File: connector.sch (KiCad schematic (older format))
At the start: 9 parts, among them J4 Conn_01x08, J5 Conn_01x06, J6 Conn_01x10, J7 Conn_01x08, U5 TA48L033

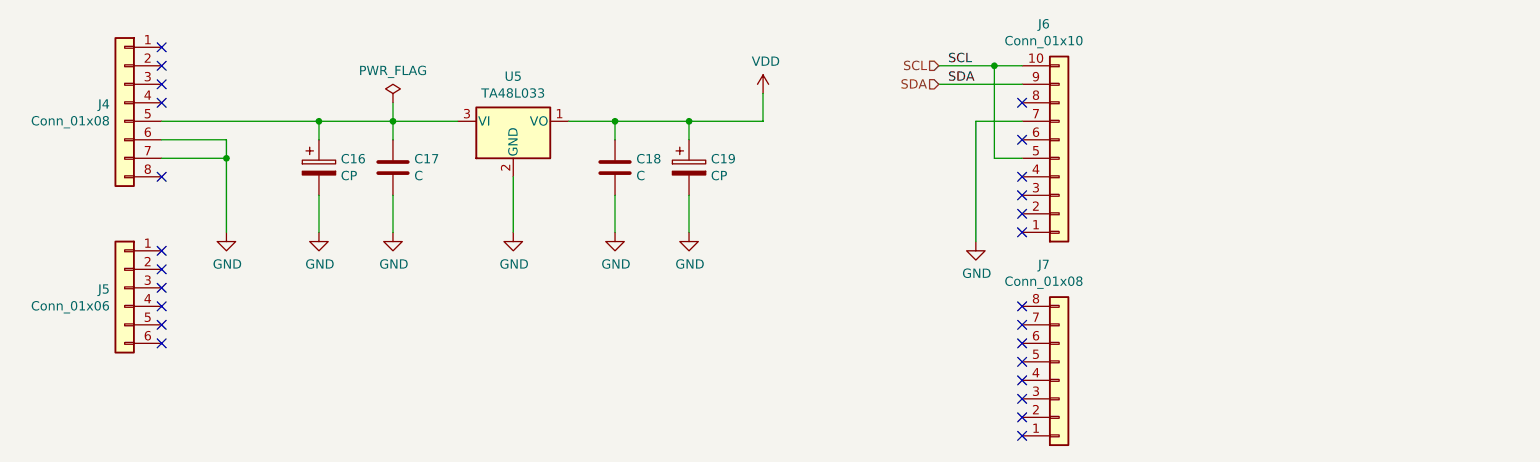
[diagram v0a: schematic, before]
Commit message: Schematics are almost done.
Audio jack is not yet.
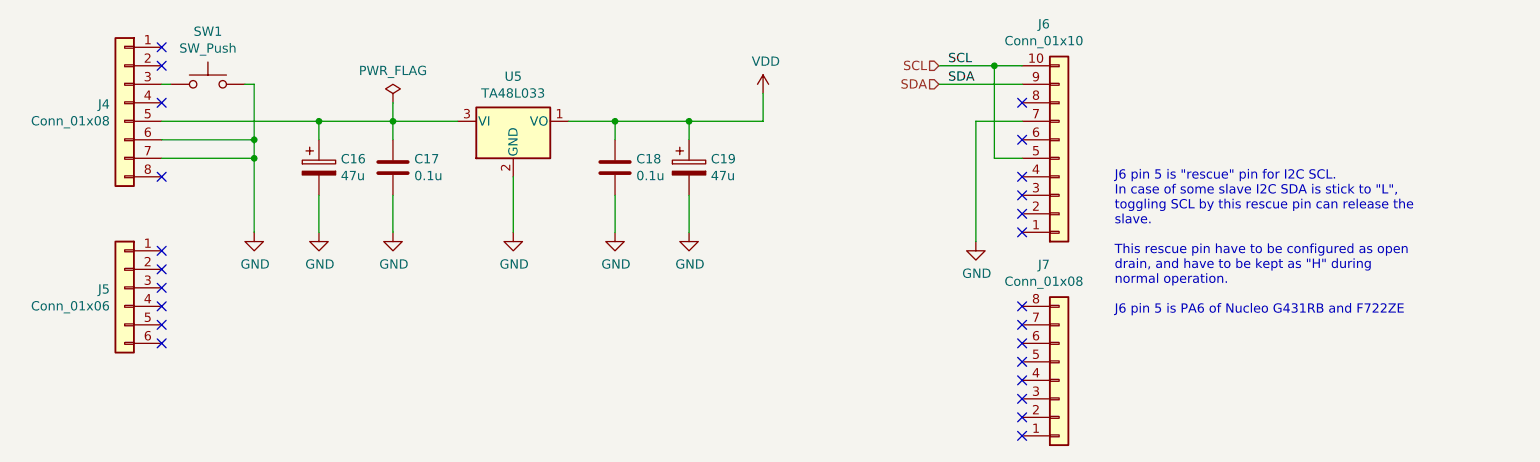
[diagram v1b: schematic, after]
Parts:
- added SW1: SW_Push, Buttons_Switches_THT:SW_PUSH_6mm_h5mm, symbol Switch:SW_Push
- C16, C19: value CP -> 47u; footprint (none) -> Capacitors_THT:CP_Radial_D8.0mm_P2.50mm
- C17, C18: value C -> 0.1u; footprint (none) -> Capacitors_THT:C_Disc_D4.7mm_W2.5mm_P5.00mm
- J4, J7: footprint (none) -> Pin_Headers:Pin_Header_Straight_1x08_Pitch2.54mm
- J5: footprint (none) -> Pin_Headers:Pin_Header_Straight_1x06_Pitch2.54mm
- J6: footprint (none) -> Pin_Headers:Pin_Header_Straight_1x10_Pitch2.54mm
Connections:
- net GND: now also SW1.2
- net at J4.3 (Pin_3): now also SW1.1
- no-connect marks 25 -> 24
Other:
- note added: "J6 pin 5 is "rescue" pin for I2C SCL.\nIn case of some slave I2C SDA is stick to "L", \ntoggling SCL by this rescue pin can release the \nslave. \n\nThis rescue pin have to be configured as open \ndrain, and have to be kept as "H" during \nnormal operation. \n\nJ6 pin 5 is PA6 of Nucleo G431RB and F722ZE"
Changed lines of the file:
@@
 F 0 "J4" H 2030 1942 50  0000 L CNN
 F 1 "Conn_01x08" H 2030 1851 50  0000 L CNN
-F 2 "" H 1950 1950 50  0001 C CNN
+F 2 "Pin_Headers:Pin_Header_Straight_1x08_Pitch2.54mm" H 1950 1950 50  0001 C CNN
 F 3 "~" H 1950 1950 50  0001 C CNN
 	1    1950 1950
@@
 F 0 "J5" H 2030 2942 50  0000 L CNN
 F 1 "Conn_01x06" H 2030 2851 50  0000 L CNN
-F 2 "" H 1950 2950 50  0001 C CNN
+F 2 "Pin_Headers:Pin_Header_Straight_1x06_Pitch2.54mm" H 1950 2950 50  0001 C CNN
 F 3 "~" H 1950 2950 50  0001 C CNN
 	1    1950 2950
@@
 F 0 "J7" H 6918 2825 50  0000 C CNN
 F 1 "Conn_01x08" H 6918 2916 50  0000 C CNN
-F 2 "" H 7000 3450 50  0001 C CNN
+F 2 "Pin_Headers:Pin_Header_Straight_1x08_Pitch2.54mm" H 7000 3450 50  0001 C CNN
 F 3 "~" H 7000 3450 50  0001 C CNN
 	1    7000 3450
@@
 F 0 "J6" H 6918 1525 50  0000 C CNN
 F 1 "Conn_01x10" H 6918 1616 50  0000 C CNN
-F 2 "" H 7000 2250 50  0001 C CNN
+F 2 "Pin_Headers:Pin_Header_Straight_1x10_Pitch2.54mm" H 7000 2250 50  0001 C CNN
 F 3 "~" H 7000 2250 50  0001 C CNN
 	1    7000 2250
@@
 P 3400 2300
 F 0 "C17" H 3515 2346 50  0000 L CNN
-F 1 "C" H 3515 2255 50  0000 L CNN
-F 2 "" H 3438 2150 50  0001 C CNN
+F 1 "0.1u" H 3515 2255 50  0000 L CNN
+F 2 "Capacitors_THT:C_Disc_D4.7mm_W2.5mm_P5.00mm" H 3438 2150 50  0001 C CNN
 F 3 "~" H 3400 2300 50  0001 C CNN
 	1    3400 2300
@@
 P 3000 2300
 F 0 "C16" H 3118 2346 50  0000 L CNN
-F 1 "CP" H 3118 2255 50  0000 L CNN
-F 2 "" H 3038 2150 50  0001 C CNN
+F 1 "47u" H 3118 2255 50  0000 L CNN
+F 2 "Capacitors_THT:CP_Radial_D8.0mm_P2.50mm" H 3038 2150 50  0001 C CNN
 F 3 "~" H 3000 2300 50  0001 C CNN
 	1    3000 2300
@@
 P 4600 2300
 F 0 "C18" H 4715 2346 50  0000 L CNN
-F 1 "C" H 4715 2255 50  0000 L CNN
-F 2 "" H 4638 2150 50  0001 C CNN
+F 1 "0.1u" H 4715 2255 50  0000 L CNN
+F 2 "Capacitors_THT:C_Disc_D4.7mm_W2.5mm_P5.00mm" H 4638 2150 50  0001 C CNN
 F 3 "~" H 4600 2300 50  0001 C CNN
 	1    4600 2300
@@
 P 5000 2300
 F 0 "C19" H 5118 2346 50  0000 L CNN
-F 1 "CP" H 5118 2255 50  0000 L CNN
-F 2 "" H 5038 2150 50  0001 C CNN
+F 1 "47u" H 5118 2255 50  0000 L CNN
+F 2 "Capacitors_THT:CP_Radial_D8.0mm_P2.50mm" H 5038 2150 50  0001 C CNN
 F 3 "~" H 5000 2300 50  0001 C CNN
 	1    5000 2300
@@
 	2150 2050 3000 2050
 Wire Wire Line
-	2150 2150 2500 2150
-Wire Wire Line
-	2500 2150 2500 2250
-Wire Wire Line
-	2150 2250 2500 2250
-Connection ~ 2500 2250
-Wire Wire Line
-	2500 2250 2500 2650
+	2150 2150 2650 2150
+Wire Wire Line
+	2650 2150 2650 2250
+Wire Wire Line
+	2150 2250 2650 2250
+Connection ~ 2650 2250
+Wire Wire Line
+	2650 2250 2650 2650
 $Comp
 L power:GND #PWR0106
 U 1 1 5F10FCB9
-P 2500 2650
-F 0 "#PWR0106" H 2500 2400 50  0001 C CNN
-F 1 "GND" H 2505 2477 50  0000 C CNN
-F 2 "" H 2500 2650 50  0001 C CNN
-F 3 "" H 2500 2650 50  0001 C CNN
-	1    2500 2650
+P 2650 2650
+F 0 "#PWR0106" H 2650 2400 50  0001 C CNN
+F 1 "GND" H 2655 2477 50  0000 C CNN
+F 2 "" H 2650 2650 50  0001 C CNN
+F 3 "" H 2650 2650 50  0001 C CNN
+	1    2650 2650
 	1    0    0    -1
 $EndComp
@@
 NoConn ~ 2150 1650
 NoConn ~ 2150 1750
-NoConn ~ 2150 1850
 NoConn ~ 2150 1950
 NoConn ~ 2150 2350
@@
 Text HLabel 6350 1850 0    50   Input ~ 0
 SDA
+Wire Wire Line
+	2650 2150 2650 1850
+Wire Wire Line
+	2650 1850 2600 1850
+Connection ~ 2650 2150
+Wire Wire Line
+	2200 1850 2150 1850
+$Comp
+L Switch:SW_Push SW1
+U 1 1 5F2D861D
+P 2400 1850
+F 0 "SW1" H 2400 2135 50  0000 C CNN
+F 1 "SW_Push" H 2400 2044 50  0000 C CNN
+F 2 "Buttons_Switches_THT:SW_PUSH_6mm_h5mm" H 2400 2050 50  0001 C CNN
+F 3 "~" H 2400 2050 50  0001 C CNN
+	1    2400 1850
+	1    0    0    -1
+$EndComp
+Text Notes 7300 3100 0    50   ~ 0
+J6 pin 5 is "rescue" pin for I2C SCL.\nIn case of some slave I2C SDA is stick to "L", \ntoggling SCL by this rescue pin can release the \nslave. \n\nThis rescue pin have to be configured as open \ndrain, and have to be kept as "H" during \nnormal operation. \n\nJ6 pin 5 is PA6 of Nucleo G431RB and F722ZE
 $EndSCHEMATC

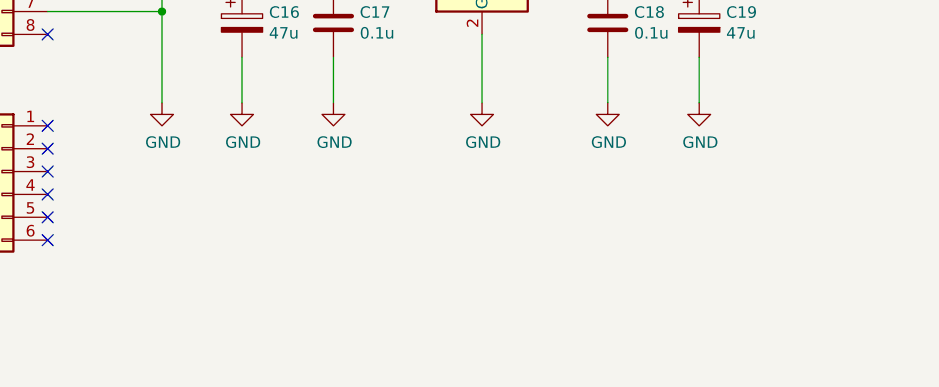
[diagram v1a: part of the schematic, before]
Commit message: Footprint done.
Added footprint of the audio jack.
The documentation link of the each IC is done.
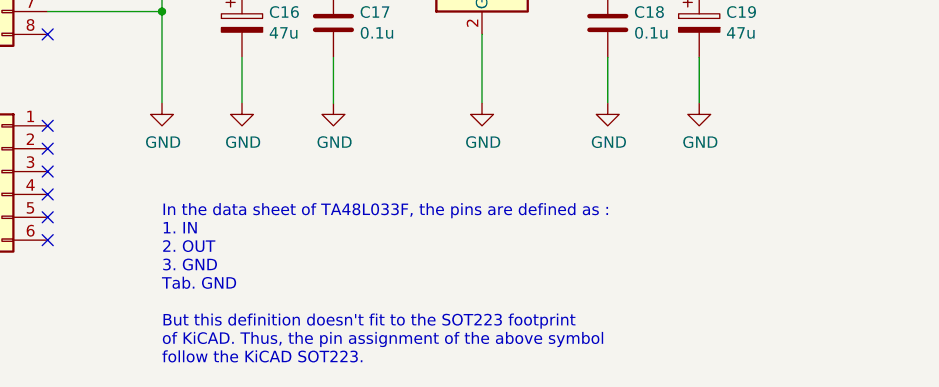
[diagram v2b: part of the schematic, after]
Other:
- note added: "In the data sheet of TA48L033F, the pins are defined as :\n1. IN\n2. OUT\n3. GND\nTab. GND\n\nBut this definition doesn't fit to the SOT223 footprint \nof KiCAD. Thus, the pin assignment of the above symbol\nfollow the KiCAD SOT223."
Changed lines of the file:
@@
 F 1 "TA48L033" H 4050 2201 50  0000 C CNN
 F 2 "TO_SOT_Packages_SMD:SOT-223-3_TabPin2" H 4050 2250 50  0001 C CNN
-F 3 "http://ww1.microchip.com/downloads/en/DeviceDoc/20005122B.pdf" H 4050 2000 50  0001 C CNN
+F 3 "https://toshiba.semicon-storage.com/jp/semiconductor/product/power-management-ics/detail.TA48L033F.html" H 4050 2000 50  0001 C CNN
 	1    4050 2050
 	1    0    0    -1
@@
 Text Notes 7300 3100 0    50   ~ 0
 J6 pin 5 is "rescue" pin for I2C SCL.\nIn case of some slave I2C SDA is stick to "L", \ntoggling SCL by this rescue pin can release the \nslave. \n\nThis rescue pin have to be configured as open \ndrain, and have to be kept as "H" during \nnormal operation. \n\nJ6 pin 5 is PA6 of Nucleo G431RB and F722ZE
+Text Notes 2650 3800 0    50   ~ 0
+In the data sheet of TA48L033F, the pins are defined as :\n1. IN\n2. OUT\n3. GND\nTab. GND\n\nBut this definition doesn't fit to the SOT223 footprint \nof KiCAD. Thus, the pin assignment of the above symbol\nfollow the KiCAD SOT223.
 $EndSCHEMATC

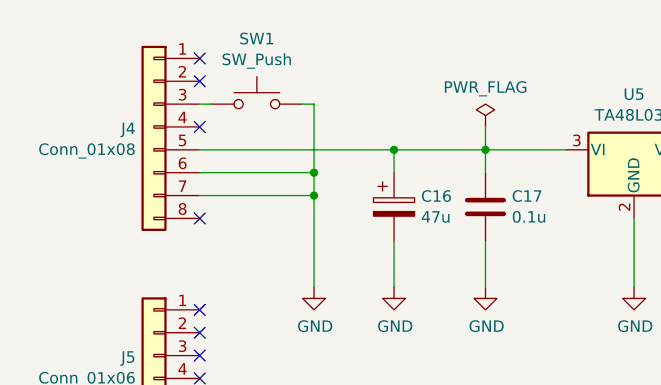
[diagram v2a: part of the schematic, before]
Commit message: All parts is on the PCB.
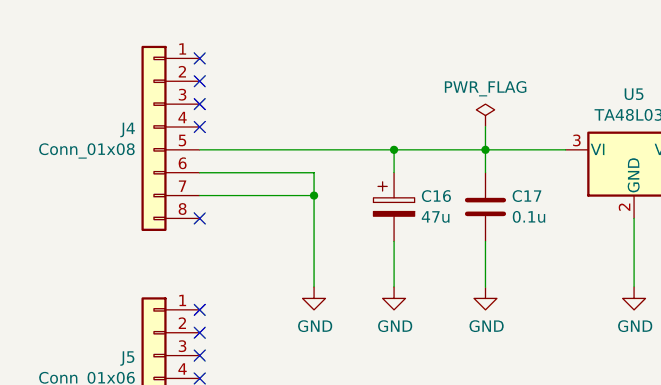
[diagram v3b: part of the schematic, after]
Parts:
- removed SW1: SW_Push, Buttons_Switches_THT:SW_PUSH_6mm_h5mm, symbol Switch:SW_Push
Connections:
- no-connect marks 24 -> 25
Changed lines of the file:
@@
 $EndComp
 $Comp
-L power:GND #PWR0101
+L power:GND #PWR032
 U 1 1 5F104015
 P 4050 2650
-F 0 "#PWR0101" H 4050 2400 50  0001 C CNN
+F 0 "#PWR032" H 4050 2400 50  0001 C CNN
 F 1 "GND" H 4055 2477 50  0000 C CNN
 F 2 "" H 4050 2650 50  0001 C CNN
@@
 $EndComp
 $Comp
-L power:GND #PWR0102
+L power:GND #PWR031
 U 1 1 5F105017
 P 3400 2650
-F 0 "#PWR0102" H 3400 2400 50  0001 C CNN
+F 0 "#PWR031" H 3400 2400 50  0001 C CNN
 F 1 "GND" H 3405 2477 50  0000 C CNN
 F 2 "" H 3400 2650 50  0001 C CNN
@@
 $EndComp
 $Comp
-L power:GND #PWR0103
+L power:GND #PWR030
 U 1 1 5F1052CF
 P 3000 2650
-F 0 "#PWR0103" H 3000 2400 50  0001 C CNN
+F 0 "#PWR030" H 3000 2400 50  0001 C CNN
 F 1 "GND" H 3005 2477 50  0000 C CNN
 F 2 "" H 3000 2650 50  0001 C CNN
@@
 $EndComp
 $Comp
-L power:GND #PWR0104
+L power:GND #PWR033
 U 1 1 5F1054A0
 P 4600 2650
-F 0 "#PWR0104" H 4600 2400 50  0001 C CNN
+F 0 "#PWR033" H 4600 2400 50  0001 C CNN
 F 1 "GND" H 4605 2477 50  0000 C CNN
 F 2 "" H 4600 2650 50  0001 C CNN
@@
 $EndComp
 $Comp
-L power:GND #PWR0105
+L power:GND #PWR034
 U 1 1 5F105733
 P 5000 2650
-F 0 "#PWR0105" H 5000 2400 50  0001 C CNN
+F 0 "#PWR034" H 5000 2400 50  0001 C CNN
 F 1 "GND" H 5005 2477 50  0000 C CNN
 F 2 "" H 5000 2650 50  0001 C CNN
@@
 	2650 2250 2650 2650
 $Comp
-L power:GND #PWR0106
+L power:GND #PWR029
 U 1 1 5F10FCB9
 P 2650 2650
-F 0 "#PWR0106" H 2650 2400 50  0001 C CNN
+F 0 "#PWR029" H 2650 2400 50  0001 C CNN
 F 1 "GND" H 2655 2477 50  0000 C CNN
 F 2 "" H 2650 2650 50  0001 C CNN
@@
 $EndComp
 $Comp
-L power:GND #PWR0107
+L power:GND #PWR036
 U 1 1 5F110343
 P 6550 2700
-F 0 "#PWR0107" H 6550 2450 50  0001 C CNN
+F 0 "#PWR036" H 6550 2450 50  0001 C CNN
 F 1 "GND" H 6555 2527 50  0000 C CNN
 F 2 "" H 6550 2700 50  0001 C CNN
@@
 NoConn ~ 6800 2150
 $Comp
-L power:VDD #PWR0108
+L power:VDD #PWR035
 U 1 1 5F116A17
 P 5400 1900
-F 0 "#PWR0108" H 5400 1750 50  0001 C CNN
+F 0 "#PWR035" H 5400 1750 50  0001 C CNN
 F 1 "VDD" H 5415 2073 50  0000 C CNN
 F 2 "" H 5400 1900 50  0001 C CNN
@@
 	5400 1900 5400 2050
 $Comp
-L power:PWR_FLAG #FLG0103
+L power:PWR_FLAG #FLG03
 U 1 1 5F17F954
 P 3400 1950
-F 0 "#FLG0103" H 3400 2025 50  0001 C CNN
+F 0 "#FLG03" H 3400 2025 50  0001 C CNN
 F 1 "PWR_FLAG" H 3400 2123 50  0000 C CNN
 F 2 "" H 3400 1950 50  0001 C CNN
@@
 Text HLabel 6350 1850 0    50   Input ~ 0
 SDA
-Wire Wire Line
-	2650 2150 2650 1850
-Wire Wire Line
-	2650 1850 2600 1850
-Connection ~ 2650 2150
-Wire Wire Line
-	2200 1850 2150 1850
-$Comp
-L Switch:SW_Push SW1
-U 1 1 5F2D861D
-P 2400 1850
-F 0 "SW1" H 2400 2135 50  0000 C CNN
-F 1 "SW_Push" H 2400 2044 50  0000 C CNN
-F 2 "Buttons_Switches_THT:SW_PUSH_6mm_h5mm" H 2400 2050 50  0001 C CNN
-F 3 "~" H 2400 2050 50  0001 C CNN
-	1    2400 1850
-	1    0    0    -1
-$EndComp
 Text Notes 7300 3100 0    50   ~ 0
 J6 pin 5 is "rescue" pin for I2C SCL.\nIn case of some slave I2C SDA is stick to "L", \ntoggling SCL by this rescue pin can release the \nslave. \n\nThis rescue pin have to be configured as open \ndrain, and have to be kept as "H" during \nnormal operation. \n\nJ6 pin 5 is PA6 of Nucleo G431RB and F722ZE
 Text Notes 2650 3800 0    50   ~ 0
 In the data sheet of TA48L033F, the pins are defined as :\n1. IN\n2. OUT\n3. GND\nTab. GND\n\nBut this definition doesn't fit to the SOT223 footprint \nof KiCAD. Thus, the pin assignment of the above symbol\nfollow the KiCAD SOT223.
+NoConn ~ 2150 1850
 $EndSCHEMATC

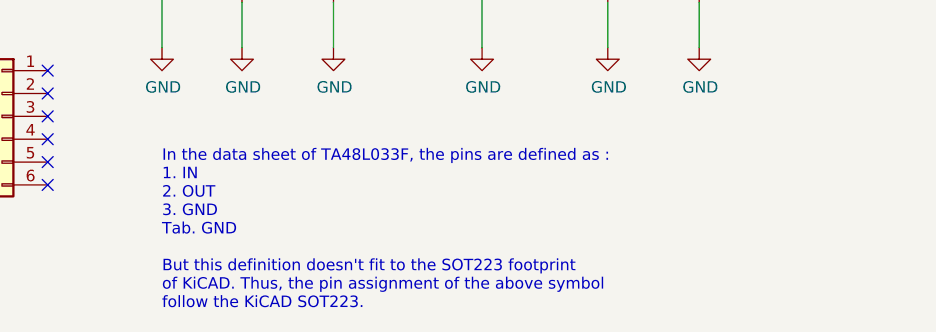
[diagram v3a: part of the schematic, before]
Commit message: Change TA48L033F foot print
Added VDD plane on the FC layer.
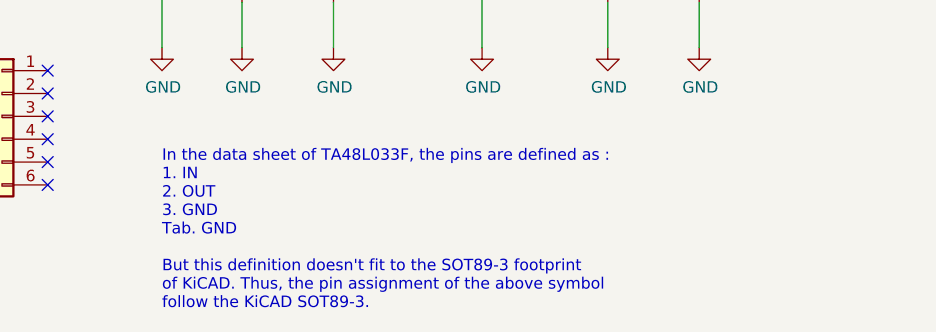
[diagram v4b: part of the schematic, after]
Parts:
- U5: footprint TO_SOT_Packages_SMD:SOT-223-3_TabPin2 -> TO_SOT_Packages_SMD:SOT-89-3_Handsoldering
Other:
- note added: "In the data sheet of TA48L033F, the pins are defined as :\n1. IN\n2. OUT\n3. GND\nTab. GND\n\nBut this definition doesn't fit to the SOT89-3 footprint \nof KiCAD. Thus, the pin assignment of the above symbol\nfollow the KiCAD SOT89-3."
- note removed: "In the data sheet of TA48L033F, the pins are defined as :\n1. IN\n2. OUT\n3. GND\nTab. GND\n\nBut this definition doesn't fit to the SOT223 footprint \nof KiCAD. Thus, the pin assignment of the above symbol\nfollow the KiCAD SOT223."
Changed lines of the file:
@@
 F 0 "U5" H 4050 2292 50  0000 C CNN
 F 1 "TA48L033" H 4050 2201 50  0000 C CNN
-F 2 "TO_SOT_Packages_SMD:SOT-223-3_TabPin2" H 4050 2250 50  0001 C CNN
+F 2 "TO_SOT_Packages_SMD:SOT-89-3_Handsoldering" H 4050 2250 50  0001 C CNN
 F 3 "https://toshiba.semicon-storage.com/jp/semiconductor/product/power-management-ics/detail.TA48L033F.html" H 4050 2000 50  0001 C CNN
 	1    4050 2050
@@
 J6 pin 5 is "rescue" pin for I2C SCL.\nIn case of some slave I2C SDA is stick to "L", \ntoggling SCL by this rescue pin can release the \nslave. \n\nThis rescue pin have to be configured as open \ndrain, and have to be kept as "H" during \nnormal operation. \n\nJ6 pin 5 is PA6 of Nucleo G431RB and F722ZE
 Text Notes 2650 3800 0    50   ~ 0
-In the data sheet of TA48L033F, the pins are defined as :\n1. IN\n2. OUT\n3. GND\nTab. GND\n\nBut this definition doesn't fit to the SOT223 footprint \nof KiCAD. Thus, the pin assignment of the above symbol\nfollow the KiCAD SOT223.
+In the data sheet of TA48L033F, the pins are defined as :\n1. IN\n2. OUT\n3. GND\nTab. GND\n\nBut this definition doesn't fit to the SOT89-3 footprint \nof KiCAD. Thus, the pin assignment of the above symbol\nfollow the KiCAD SOT89-3.
 NoConn ~ 2150 1850
 $EndSCHEMATC
